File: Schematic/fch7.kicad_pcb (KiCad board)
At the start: 4 copper layers, 39 x 40.9 mm, 155 parts, among them IC1 MP9943AGQ-Z, IC2 MP9943AGQ-Z, IC4 ICM-42688-P, IC5 MPU-6500, J1 U.FL-R-SMT-1_01_, J11 PIN2216, J12 PIN2216, J2 PIN2216, J3 PIN2216, J4 PIN2216, J5 PIN2216, J6 PIN2216, J7 PIN2216, J8 PIN2216, J9 PIN2216, U1 ME6217C33M5G, U10 HDGC1002WR-S-4P, U11 HDGC1002WR-S-4P, U12 E28-2G4M27SX, U14 MIA-M10Q, U15 HDGC1002WR-S-6P, U16 HDGC1002WR-S-8P, U17 HDGC1002WR-S-8P, U18 MAX40200ANS, U19 STM32H743VIHx, U2 ME6217C33M5G, U3 LDO-1.8v, U4 QMC5883L, U5 SPL06-001, U6 CSNP1GCR01-BOW, U7 HDGC1002WR-S-6P, U8 HDGC1002WR-S-4P, U9 HDGC1002WR-S-4P, Y1 8MHz, Y2 CM8V-T1A

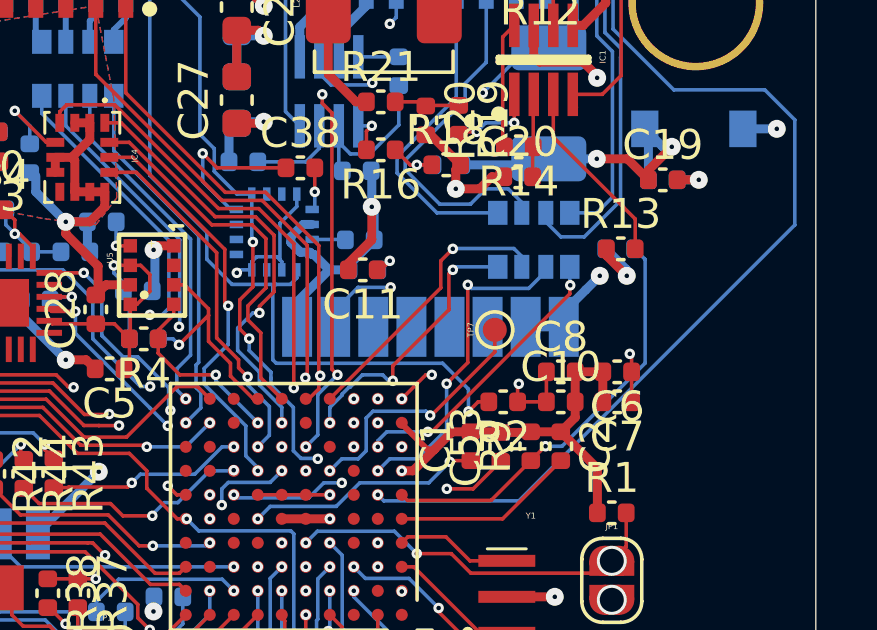
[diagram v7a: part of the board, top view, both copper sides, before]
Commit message: update: modify net connections and add unconnected nets in PCB design
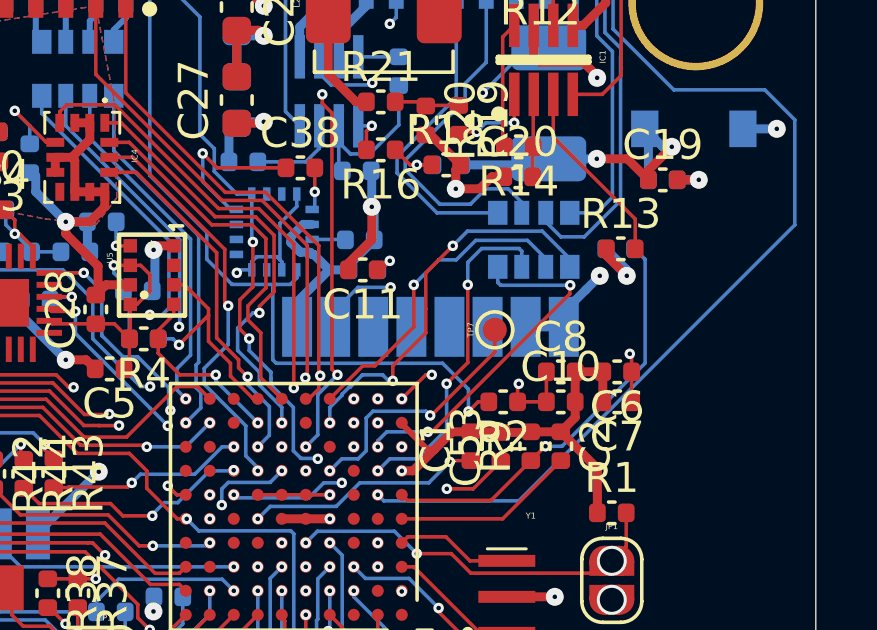
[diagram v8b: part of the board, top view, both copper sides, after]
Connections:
- net Net-(U4-C1) renamed /Sensors/C1
- RN2 pad 5: PWM_1 -> PWM_4
- RN2 pad 6: PWM_2 -> PWM_3
- RN2 pad 7: PWM_3 -> PWM_2
- RN2 pad 8: PWM_4 -> PWM_1
- U19 pad A1: (no net) -> unconnected-(U19-PC14-PadA1)
- U19 pad B2: (no net) -> unconnected-(U19-VBAT-PadB2)
- U19 pad C9: (no net) -> unconnected-(U19-PA9-PadC9)
- U19 pad D10: (no net) -> unconnected-(U19-PA10-PadD10)
- U19 pad E2: (no net) -> unconnected-(U19-PC2_C-PadE2)
- U19 pad F3: (no net) -> unconnected-(U19-PC3_C-PadF3)
- U19 pad G3: (no net) -> unconnected-(U19-PA4-PadG3)
- U19 pad K8: (no net) -> unconnected-(U19-PB12-PadK8)
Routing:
- net PWM_1: track 9.23 -> 13.2 mm
- net PWM_4: track 9.59 -> 12.1 mm
- net PWM_2: track 9.48 -> 10.8 mm
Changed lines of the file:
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@@
 	(net 13 "9V_BEC")
 	(net 14 "VBAT")
-	(net 15 "Net-(U4-C1)")
+	(net 15 "/Sensors/C1")
 	(net 16 "VDD_RECV")
 	(net 17 "5V_USB")
@@
 	(net 187 "/Blackbox_led/LED_MCU_R")
 	(net 188 "/rf_rx/LED_RECV")
+	(net 189 "unconnected-(U19-PB12-PadK8)")
+	(net 190 "unconnected-(U19-VBAT-PadB2)")
+	(net 191 "unconnected-(U19-PC3_C-PadF3)")
+	(net 192 "unconnected-(U19-PC2_C-PadE2)")
+	(net 193 "unconnected-(U19-PA10-PadD10)")
+	(net 194 "unconnected-(U19-PA4-PadG3)")
+	(net 195 "unconnected-(U19-PA9-PadC9)")
+	(net 196 "unconnected-(U19-PC14-PadA1)")
 	(footprint "fch7:TestPoint_Pad_D0.8"
 		(layer "F.Cu")
@@
 			(property pad_prop_bga)
 			(layers "F.Cu" "F.Mask" "F.Paste")
+			(net 196 "unconnected-(U19-PC14-PadA1)")
 			(pinfunction "PC14")
 			(pintype "bidirectional+no_connect")
@@
 			(property pad_prop_bga)
 			(layers "F.Cu" "F.Mask" "F.Paste")
+			(net 190 "unconnected-(U19-VBAT-PadB2)")
 			(pinfunction "VBAT")
 			(pintype "power_in+no_connect")
@@
 			(property pad_prop_bga)
 			(layers "F.Cu" "F.Mask" "F.Paste")
+			(net 195 "unconnected-(U19-PA9-PadC9)")
 			(pinfunction "PA9")
 			(pintype "bidirectional+no_connect")
@@
 			(property pad_prop_bga)
 			(layers "F.Cu" "F.Mask" "F.Paste")
+			(net 193 "unconnected-(U19-PA10-PadD10)")
 			(pinfunction "PA10")
 			(pintype "bidirectional+no_connect")
@@
 			(property pad_prop_bga)
 			(layers "F.Cu" "F.Mask" "F.Paste")
+			(net 192 "unconnected-(U19-PC2_C-PadE2)")
 			(pinfunction "PC2_C")
 			(pintype "bidirectional+no_connect")
@@
 			(property pad_prop_bga)
 			(layers "F.Cu" "F.Mask" "F.Paste")
+			(net 191 "unconnected-(U19-PC3_C-PadF3)")
 			(pinfunction "PC3_C")
 			(pintype "bidirectional+no_connect")
@@
 			(property pad_prop_bga)
 			(layers "F.Cu" "F.Mask" "F.Paste")
+			(net 194 "unconnected-(U19-PA4-PadG3)")
 			(pinfunction "PA4")
 			(pintype "bidirectional+no_connect")
@@
 			(property pad_prop_bga)
 			(layers "F.Cu" "F.Mask" "F.Paste")
+			(net 189 "unconnected-(U19-PB12-PadK8)")
 			(pinfunction "PB12")
 			(pintype "bidirectional+no_connect")
@@
 			(layers "B.Cu" "B.Mask" "B.Paste")
 			(roundrect_rratio 0.25)
-			(net 15 "Net-(U4-C1)")
+			(net 15 "/Sensors/C1")
 			(pintype "passive")
 		)
@@
 			(size 0.65 0.8)
 			(layers "B.Cu" "B.Mask" "B.Paste")
-			(net 42 "PWM_1")
+			(net 72 "PWM_4")
 			(pinfunction "5")
 			(pintype "passive")
@@
 			(size 0.5 0.8)
 			(layers "B.Cu" "B.Mask" "B.Paste")
-			(net 63 "PWM_2")
+			(net 50 "PWM_3")
 			(pinfunction "6")
 			(pintype "passive")
@@
 			(size 0.5 0.8)
 			(layers "B.Cu" "B.Mask" "B.Paste")
-			(net 50 "PWM_3")
+			(net 63 "PWM_2")
 			(pinfunction "7")
 			(pintype "passive")
@@
 			(size 0.65 0.8)
 			(layers "B.Cu" "B.Mask" "B.Paste")
-			(net 72 "PWM_4")
+			(net 42 "PWM_1")
 			(pinfunction "8")
 			(pintype "passive")
@@
 			(size 0.25 0.45)
 			(layers "B.Cu" "B.Mask" "B.Paste")
-			(net 15 "Net-(U4-C1)")
+			(net 15 "/Sensors/C1")
 			(pinfunction "C1")
 			(pintype "input")
@@
 	)
 	(segment
-		(start 91.371 74.929)
-		(end 91.5 74.8)
+		(start 90.6 76.9)
+		(end 90.6 76.1)
 		(width 0.12)
 		(layer "F.Cu")
@@
 	)
 	(segment
-		(start 89.5 78.5)
-		(end 89.5 78)
+		(start 89.5 78)
+		(end 89.5 78.5)
 		(width 0.12)
 		(layer "F.Cu")
@@
 	)
 	(segment
-		(start 91.371 76.129)
-		(end 91.371 74.929)
+		(start 89.5 78)
+		(end 90.6 76.9)
 		(width 0.12)
 		(layer "F.Cu")
@@
 	)
 	(segment
-		(start 89.5 78)
-		(end 91.371 76.129)
+		(start 90.6 74.9)
+		(end 91.5 74)
+		(width 0.12)
+		(layer "F.Cu")
+		(net 42)
+	)
+	(segment
+		(start 90.6 76.1)
+		(end 90.6 74.9)
 		(width 0.12)
 		(layer "F.Cu")
@@
 	)
 	(via
-		(at 91.5 74.8)
+		(at 91.5 74)
 		(size 0.35)
 		(drill 0.15)
@@
 	)
 	(segment
-		(start 91.5 74.8)
-		(end 91.6 74.7)
+		(start 91.5 74)
+		(end 91.989 73.511)
 		(width 0.12)
 		(layer "B.Cu")
@@
 	)
 	(segment
+		(start 95.4 74.428)
+		(end 95.4 74.7)
+		(width 0.12)
+		(layer "B.Cu")
+		(net 42)
+	)
+	(segment
 		(start 89.161295 78.300352)
 		(end 88.489116 78.300352)
@@
 	)
 	(segment
+		(start 91.989 73.511)
+		(end 94.483 73.511)
+		(width 0.12)
+		(layer "B.Cu")
+		(net 42)
+	)
+	(segment
 		(start 89.5 78.5)
 		(end 89.360943 78.5)
@@
 	)
 	(segment
+		(start 94.483 73.511)
+		(end 95.4 74.428)
+		(width 0.12)
+		(layer "B.Cu")
+		(net 42)
+	)
+	(segment
 		(start 89.360943 78.5)
 		(end 89.161295 78.300352)
@@
 	)
 	(segment
-		(start 91.6 74.7)
-		(end 93 74.7)
-		(width 0.12)
-		(layer "B.Cu")
-		(net 42)
-	)
-	(segment
 		(start 86.200001 78.74)
 		(end 86.200001 73.922965)
@@
 	)
 	(segment
+		(start 92 74.553)
+		(end 92.464 74.089)
+		(width 0.12)
+		(layer "B.Cu")
+		(net 50)
+	)
+	(segment
 		(start 91.295441 78.595441)
 		(end 91.295441 80.119446)
@@
 	)
 	(segment
+		(start 93.8 74.18)
+		(end 93.8 74.7)
+		(width 0.12)
+		(layer "B.Cu")
+		(net 50)
+	)
+	(segment
 		(start 90.314887 81.1)
 		(end 89.4 81.1)
@@
 	(segment
 		(start 92 75.3)
-		(end 92.119484 75.419484)
+		(end 92 74.553)
 		(width 0.12)
 		(layer "B.Cu")
@@
 	)
 	(segment
-		(start 92.119484 75.419484)
-		(end 94.030516 75.419484)
+		(start 93.709 74.089)
+		(end 93.8 74.18)
 		(width 0.12)
 		(layer "B.Cu")
@@
 	)
 	(segment
-		(start 94.6 74.7)
-		(end 94.6 74.85)
+		(start 92.464 74.089)
+		(end 93.709 74.089)
 		(width 0.12)
 		(layer "B.Cu")
@@
 	)
 	(segment
-		(start 94.6 74.85)
-		(end 94.030516 75.419484)
-		(width 0.12)
-		(layer "B.Cu")
-		(net 50)
-	)
-	(segment
 		(start 89.4 81.1)
 		(end 89 81.5)
@@
 	)
 	(segment
-		(start 91.1 74.5)
-		(end 91.5 74.1)
+		(start 88.9 78)
+		(end 88.5 78)
+		(width 0.12)
+		(layer "F.Cu")
+		(net 63)
+	)
+	(segment
+		(start 90.2 76.7)
+		(end 88.9 78)
 		(width 0.12)
 		(layer "F.Cu")
@@
 	)
 	(segment
-		(start 91.1 75.4)
-		(end 91.1 74.5)
+		(start 90.2 75.3)
+		(end 90.2 76.7)
 		(width 0.12)
 		(layer "F.Cu")
@@
 	)
 	(segment
-		(start 87.4 79.1)
-		(end 91.1 75.4)
+		(start 88.5 78)
+		(end 87.4 79.1)
 		(width 0.12)
 		(layer "F.Cu")
@@
 	)
 	(via
-		(at 91.5 74.1)
+		(at 90.2 75.3)
 		(size 0.35)
 		(drill 0.15)
@@
 	)
 	(segment
-		(start 91.511 74.089)
-		(end 91.5 74.1)
+		(start 94.6 74.428)
+		(end 94.6 74.7)
+		(width 0.12)
+		(layer "B.Cu")
+		(net 63)
+	)
+	(segment
+		(start 91.615 74.467224)
+		(end 92.264224 73.818)
+		(width 0.12)
+		(layer "B.Cu")
+		(net 63)
+	)
+	(segment
+		(start 93.99 73.818)
+		(end 94.6 74.428)
 		(width 0.12)
 		(layer "B.Cu")
@@
 	)
 	(segment
-		(start 93.8 74.353)
-		(end 93.536 74.089)
+		(start 91.032776 74.467224)
+		(end 91.615 74.467224)
 		(width 0.12)
 		(layer "B.Cu")
@@
 	)
 	(segment
-		(start 93.8 74.7)
-		(end 93.8 74.353)
+		(start 92.264224 73.818)
+		(end 93.99 73.818)
 		(width 0.12)
 		(layer "B.Cu")
@@
 	)
 	(segment
-		(start 93.536 74.089)
-		(end 91.511 74.089)
+		(start 90.2 75.3)
+		(end 91.032776 74.467224)
 		(width 0.12)
 		(layer "B.Cu")
@@
 	)
 	(segment
-		(start 95.4 75.205048)
-		(end 95.4 74.7)
+		(start 93.094124 75.314124)
+		(end 95.414124 75.314124)
 		(width 0.12)
 		(layer "B.Cu")
@@
 		(width 0.12)
 		(layer "B.Cu")
+		(net 72)
+	)
+	(segment
+		(start 93 74.7)
+		(end 93 75.22)
+		(width 0.12)
+		(layer "B.Cu")
+		(net 72)
+	)
+	(segment
+		(start 93 75.22)
+		(end 93.094124 75.314124)
+		(width 0.12)
+		(layer "B.Cu")
